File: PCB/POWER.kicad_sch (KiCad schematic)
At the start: 32 parts, among them IC100 AP63203WU-7, J100 2604-3102, Q100 CSD19537Q3, Q101 BSS138, U100 TPS26631RGE

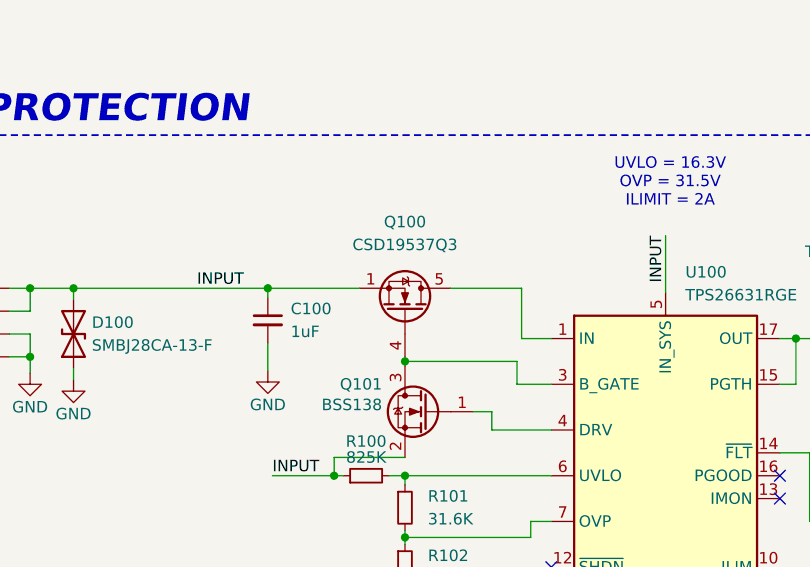
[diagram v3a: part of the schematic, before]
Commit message: PCB acabada con labels
Se agrego:
- Planos de tierra
- Stitching vias
- Labels indicadores para todo los conectores

Se corrigio:
- Errores de librerias de footprint - TPS26631RGE
- Pines sin conectarse
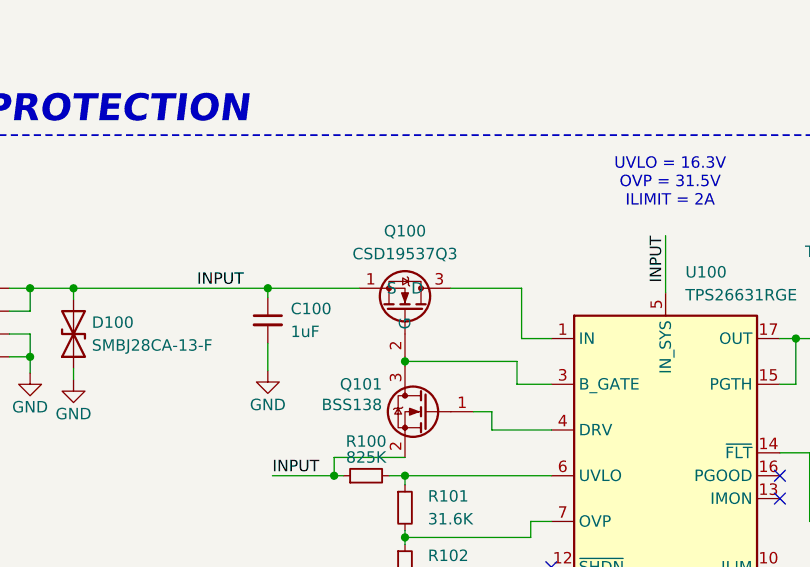
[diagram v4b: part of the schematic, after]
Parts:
- removed Q100: CSD19537Q3, Package_SON:VSON-8_3.3x3.3mm_P0.65mm_NexFET, symbol Transistor_FET:CSD19537Q3
- added Q100: CSD19537Q3, CSD19537Q3:CSD19537Q3, symbol CSD19537Q3:CSD19537Q3
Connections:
- net INPUT: now also Q100.1 (S)
- net at U100.1 (IN), U100.2 (IN): now also Q100.3 (D)
- net at Q101.3 (D), U100.3 (B_GATE): now also Q100.2 (G)
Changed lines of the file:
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@@
 	(wire
 		(pts
+			(xy 84.582 63.754) (xy 92.456 63.754)
+		)
+		(stroke
+			(width 0)
+			(type default)
+		)
+	)
+	(wire
+		(pts
 			(xy 64.262 69.85) (xy 64.262 72.898)
 		)
@@
 	(wire
 		(pts
-			(xy 84.582 63.754) (xy 92.456 63.754)
-		)
-		(stroke
-			(width 0)
-			(type default)
-		)
-	)
-	(wire
-		(pts
 			(xy 250.19 58.42) (xy 250.19 61.722)
 		)
@@
 	)
 	(symbol
-		(lib_id "Transistor_FET:CSD19537Q3")
-		(at 79.502 66.294 270)
-		(mirror x)
-		(unit 1)
-		(exclude_from_sim no)
-		(in_bom yes)
-		(on_board yes)
-		(dnp no)
-		(property "Reference" "Q100"
-			(at 79.502 56.388 90)
-			(effects
-				(font
-					(size 1.27 1.27)
-				)
-			)
-		)
-		(property "Value" "CSD19537Q3"
-			(at 79.502 58.928 90)
-			(effects
-				(font
-					(size 1.27 1.27)
-				)
-			)
-		)
-		(property "Footprint" "Package_SON:VSON-8_3.3x3.3mm_P0.65mm_NexFET"
-			(at 77.597 61.214 0)
-			(effects
-				(font
-					(size 1.27 1.27)
-					(italic yes)
-				)
-				(justify left)
-				(hide yes)
-			)
-		)
-		(property "Datasheet" "http://www.ti.com/lit/ds/symlink/csd19537q3.pdf"
-			(at 75.692 61.214 0)
-			(effects
-				(font
-					(size 1.27 1.27)
-				)
-				(justify left)
-				(hide yes)
-			)
-		)
-		(property "Description" "50A Id, 100V Vds, NexFET N-Channel Power MOSFET, 13mOhm Ron, Qg Typ 16.0nC, VSON8 3.3x3.3mm"
-			(at 79.502 66.294 0)
-			(effects
-				(font
-					(size 1.27 1.27)
-				)
-				(hide yes)
-			)
-		)
-		(property "LCSC" "C478469"
-			(at 79.502 66.294 90)
-			(effects
-				(font
-					(size 1.27 1.27)
-				)
-				(hide yes)
-			)
-		)
-		(pin "3"
-		)
-		(pin "1"
-		)
-		(pin "2"
-		)
-		(pin "5"
-		)
-		(pin "4"
-		)
-		(instances
-			(project ""
-				(path "/118ffa26-3c65-424a-af71-04338c4de0b0/e2751aaa-40ab-491e-8724-b4cb7cd2712b"
-					(reference "Q100")
-					(unit 1)
-				)
-			)
-		)
-	)
-	(symbol
 		(lib_id "power:GND")
 		(at 157.734 83.82 0)
@@
 					(unit 1)
 				)
+			)
+		)
+	)
+	(symbol
+		(lib_id "CSD19537Q3:CSD19537Q3")
+		(at 79.502 81.534 270)
+		(mirror x)
+		(unit 1)
+		(exclude_from_sim no)
+		(in_bom yes)
+		(on_board yes)
+		(dnp no)
+		(property "Reference" "Q100"
+			(at 79.502 57.404 90)
+			(effects
+				(font
+					(size 1.27 1.27)
+				)
+			)
+		)
+		(property "Value" "CSD19537Q3"
+			(at 79.502 59.944 90)
+			(effects
+				(font
+					(size 1.27 1.27)
+				)
+			)
+		)
+		(property "Footprint" "CSD19537Q3:CSD19537Q3"
+			(at -15.418 59.944 0)
+			(effects
+				(font
+					(size 1.27 1.27)
+				)
+				(justify left top)
+				(hide yes)
+			)
+		)
+		(property "Datasheet" "http://www.ti.com/lit/gpn/csd19537q3"
+			(at -115.418 59.944 0)
+			(effects
+				(font
+					(size 1.27 1.27)
+				)
+				(justify left top)
+				(hide yes)
+			)
+		)
+		(property "Description" "100V, N ch NexFET MOSFET, single SON3x3, 14.5mOhm"
+			(at 79.502 81.534 0)
+			(effects
+				(font
+					(size 1.27 1.27)
+				)
+				(hide yes)
+			)
+		)
+		(property "Height" ""
+			(at -315.418 59.944 0)
+			(effects
+				(font
+					(size 1.27 1.27)
+				)
+				(justify left top)
+				(hide yes)
+			)
+		)
+		(property "Mouser Part Number" "595-CSD19537Q3"
+			(at -415.418 59.944 0)
+			(effects
+				(font
+					(size 1.27 1.27)
+				)
+				(justify left top)
+				(hide yes)
+			)
+		)
+		(property "Mouser Price/Stock" "https://www.mouser.co.uk/ProductDetail/Texas-Instruments/CSD19537Q3?qs=kFLL9AfgRSA2baK1OoK3Jg%3D%3D"
+			(at -515.418 59.944 0)
+			(effects
+				(font
+					(size 1.27 1.27)
+				)
+				(justify left top)
+				(hide yes)
+			)
+		)
+		(property "Manufacturer_Name" "Texas Instruments"
+			(at -615.418 59.944 0)
+			(effects
+				(font
+					(size 1.27 1.27)
+				)
+				(justify left top)
+				(hide yes)
+			)
+		)
+		(property "Manufacturer_Part_Number" "CSD19537Q3"
+			(at -715.418 59.944 0)
+			(effects
+				(font
+					(size 1.27 1.27)
+				)
+				(justify left top)
+				(hide yes)
+			)
+		)
+		(property "LCSC" "C478469"
+			(at 79.502 81.534 90)
+			(effects
+				(font
+					(size 1.27 1.27)
+				)
+				(hide yes)
+			)
+		)
+		(pin "1"
+		)
+		(pin "3"
+		)
+		(pin "2"
+		)
+		(instances
+			(project ""
+				(path "/118ffa26-3c65-424a-af71-04338c4de0b0/e2751aaa-40ab-491e-8724-b4cb7cd2712b"
+					(reference "Q100")
+					(unit 1)
+				)

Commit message: Edicion de archivos para JLCPCB
Se ha realizado:
- Cambio de footprint de capacitor 1mF
- Edicion de algunos value references
- Creación de archivos para JLCPCB
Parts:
- C102: footprint Capacitor_SMD:CP_Elec_16x17.5 -> VKMI1701H102MV:VKMI1701H102MV
- Q101: LCSC C7420339 -> C40912
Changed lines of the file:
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@@
 			)
 		)
-		(property "Footprint" "Capacitor_SMD:CP_Elec_16x17.5"
+		(property "Footprint" "VKMI1701H102MV:VKMI1701H102MV"
 			(at 128.778 73.152 0)
 			(effects
@@
 			)
 		)
-		(property "LCSC" "C7420339"
+		(property "LCSC" "C40912"
 			(at 82.042 77.47 0)
 			(effects

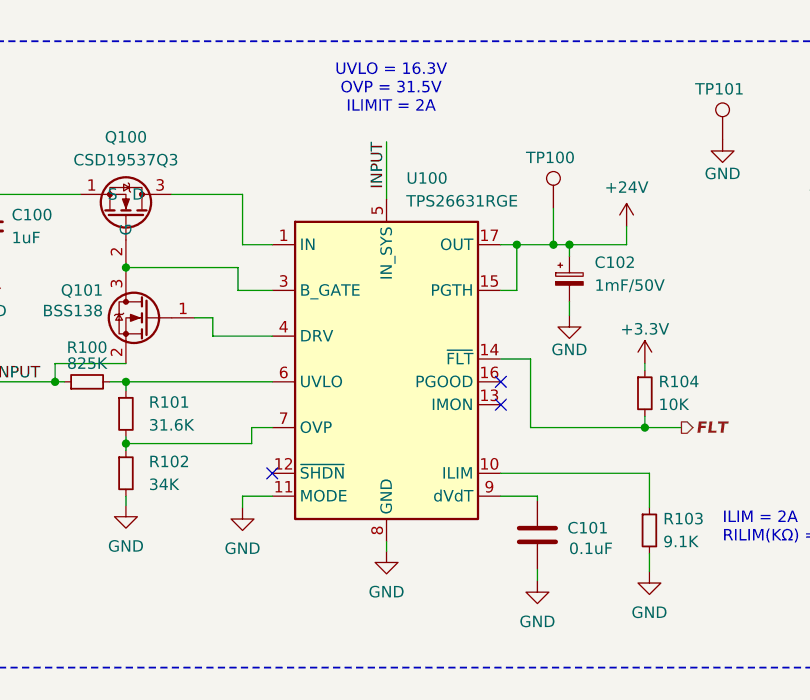
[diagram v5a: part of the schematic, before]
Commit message: Cambio de footprint del eFuse
- Se cambio el footprint del eFuse debido a que el actual no hay stock en JLCPCB
- Se creo de nuevo los archivos de configuracion de JLCPCB
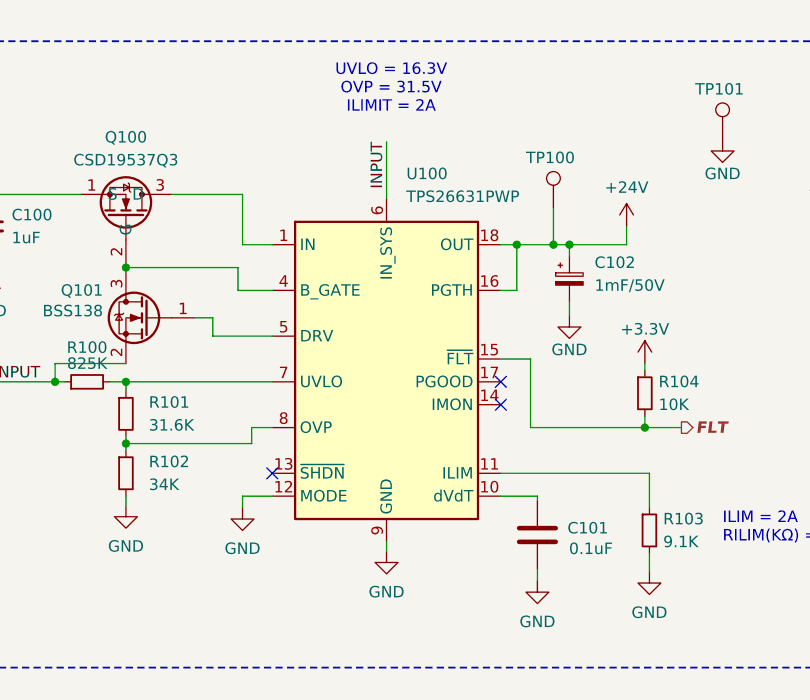
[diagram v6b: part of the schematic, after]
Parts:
- removed U100: TPS26631RGE, Package_DFN_QFN:Texas_RGE0024H_VQFN-24-1EP_4x4mm_P0.5mm_EP2.7x2.7mm_ThermalVias, symbol Power_Management:TPS26631RGE
- added U100: TPS26631PWP, Package_SO:HTSSOP-20-1EP_4.4x6.5mm_P0.65mm_EP3.4x6.5mm_Mask2.96x2.96mm_ThermalVias, symbol Power_Management:TPS26631PWP
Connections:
- net +24V: now also U100.16 (PGTH), U100.18 (OUT), U100.19 (OUT), U100.20 (OUT)
- net FLT: now also U100.15 (~{FLT})
- net GND: now also U100.12 (MODE), U100.21 (GND), U100.9 (GND)
- net INPUT: now also U100.6 (IN_SYS)
- net at R103.1: now also U100.11 (ILIM)
- net at R100.2, R101.1: now also U100.7 (UVLO)
- net at R101.2, R102.1: now also U100.8 (OVP)
- net at Q100.3 (D): now also U100.1 (IN), U100.2 (IN), U100.3 (IN)
- net at Q100.2 (G), Q101.3 (D): now also U100.4 (B_GATE)
- net at Q101.1 (G): now also U100.5 (DRV)
- net at C101.2: now also U100.10 (dVdT)
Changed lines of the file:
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@@
+	)
+	(symbol
+		(lib_id "Power_Management:TPS26631PWP")
+		(at 108.458 82.042 0)
+		(unit 1)
+		(exclude_from_sim no)
+		(in_bom yes)
+		(on_board yes)
+		(dnp no)
+		(fields_autoplaced yes)
+		(property "Reference" "U100"
+			(at 110.6521 61.468 0)
+			(effects
+				(font
+					(size 1.27 1.27)
+				)
+				(justify left)
+			)
+		)
+		(property "Value" "TPS26631PWP"
+			(at 110.6521 64.008 0)
+			(effects
+				(font
+					(size 1.27 1.27)
+				)
+				(justify left)
+			)
+		)
+		(property "Footprint" "Package_SO:HTSSOP-20-1EP_4.4x6.5mm_P0.65mm_EP3.4x6.5mm_Mask2.96x2.96mm_ThermalVias"
+			(at 108.458 113.792 0)
+			(effects
+				(font
+					(size 1.27 1.27)
+				)
+				(hide yes)
+			)
+		)
+		(property "Datasheet" "https://www.ti.com/lit/ds/symlink/tps2663.pdf"
+			(at 98.298 61.722 0)
+			(effects
+				(font
+					(size 1.27 1.27)
+				)
+				(hide yes)
+			)
+		)
+		(property "Description" "60V, 6A Power Limiting, Surge Protection Industrial eFuse, Adjustable Overvoltage cut-off, Active Current Limiting with Pulse current support, HTTSOP-20"
+			(at 108.458 82.042 0)
+			(effects
+				(font
+					(size 1.27 1.27)
+				)
+				(hide yes)
+			)
+		)
+		(property "LCSC" "C2832195"
+			(at 108.458 82.042 0)
+			(effects
+				(font
+					(size 1.27 1.27)
+				)
+				(hide yes)
+			)
+		)
+		(pin "12"
+		)
+		(pin "21"
+		)
+		(pin "5"
+		)
+		(pin "6"
+		)
+		(pin "7"
+		)
+		(pin "15"
+		)
+		(pin "14"
+		)
+		(pin "19"
+		)
+		(pin "9"
+		)
+		(pin "18"
+		)
+		(pin "10"
+		)
+		(pin "20"
+		)
+		(pin "8"
+		)
+		(pin "16"
+		)
+		(pin "1"
+		)
+		(pin "2"
+		)
+		(pin "3"
+		)
+		(pin "11"
+		)
+		(pin "4"
+		)
+		(pin "17"
+		)
+		(pin "13"
+		)
+		(instances
+			(project ""
+				(path "/118ffa26-3c65-424a-af71-04338c4de0b0/e2751aaa-40ab-491e-8724-b4cb7cd2712b"
+					(reference "U100")
+					(unit 1)
+				)
+			)
+		)
 	)
 	(symbol
@@
 					(unit 1)
 				)
-			)
-		)
-	)
-	(symbol
-		(lib_id "Power_Management:TPS26631RGE")
-		(at 108.458 82.042 0)
-		(unit 1)
-		(exclude_from_sim no)
-		(in_bom yes)
-		(on_board yes)
-		(dnp no)
-		(fields_autoplaced yes)
-		(property "Reference" "U100"
-			(at 110.6521 61.976 0)
-			(effects
-				(font
-					(size 1.27 1.27)
-				)
-				(justify left)
-			)
-		)
-		(property "Value" "TPS26631RGE"
-			(at 110.6521 64.516 0)
-			(effects
-				(font
-					(size 1.27 1.27)
-				)
-				(justify left)
-			)
-		)
-		(property "Footprint" "Package_DFN_QFN:Texas_RGE0024H_VQFN-24-1EP_4x4mm_P0.5mm_EP2.7x2.7mm_ThermalVias"
-			(at 108.458 113.792 0)
-			(effects
-				(font
-					(size 1.27 1.27)
-				)
-				(hide yes)
-			)
-		)
-		(property "Datasheet" "https://www.ti.com/lit/ds/symlink/tps2663.pdf"
-			(at 98.298 61.722 0)
-			(effects
-				(font
-					(size 1.27 1.27)
-				)
-				(hide yes)
-			)
-		)
-		(property "Description" "60V, 6A Power Limiting, Surge Protection Industrial eFuse, Adjustable Overvoltage cut-off, Active Current Limiting with Pulse current support, VQFN-24"
-			(at 108.458 82.042 0)
-			(effects
-				(font
-					(size 1.27 1.27)
-				)
-				(hide yes)
-			)
-		)
-		(property "LCSC" "C1850273"
-			(at 108.458 82.042 0)
-			(effects
-				(font
-					(size 1.27 1.27)
-				)
-				(hide yes)
-			)
-		)
-		(pin "11"
-		)
-		(pin "6"
-		)
-		(pin "10"
-		)
-		(pin "21"
-		)
-		(pin "23"
-		)
-		(pin "12"
-		)
-		(pin "9"
-		)
-		(pin "24"
-		)
-		(pin "17"
-		)
-		(pin "2"
-		)
-		(pin "13"
-		)
-		(pin "4"
-		)
-		(pin "7"
-		)
-		(pin "8"
-		)
-		(pin "1"
-		)
-		(pin "19"
-		)
-		(pin "22"
-		)
-		(pin "14"
-		)
-		(pin "18"
-		)
-		(pin "25"
-		)
-		(pin "5"
-		)
-		(pin "15"
-		)
-		(pin "3"
-		)
-		(pin "16"
-		)
-		(pin "20"
-		)
-		(instances
-			(project "PCB-Cuarto"
-				(path "/118ffa26-3c65-424a-af71-04338c4de0b0/e2751aaa-40ab-491e-8724-b4cb7cd2712b"
-					(reference "U100")
-					(unit 1)
-				)

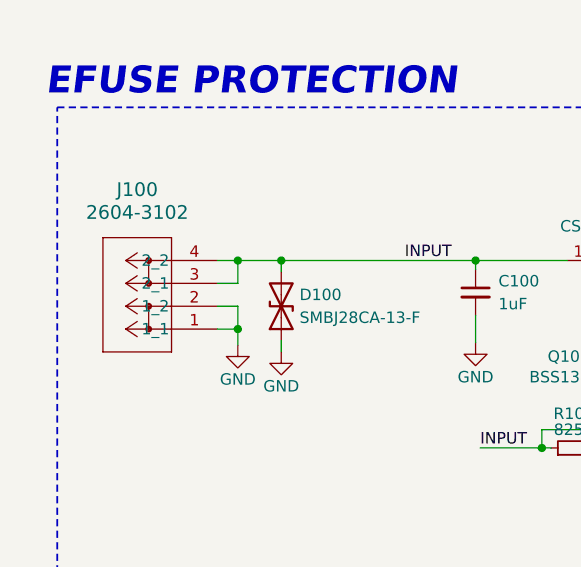
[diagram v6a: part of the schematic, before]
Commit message: Change Placement
Se ha cambiado el placement total para obtener una mejor posicion de conexion de los perifericos
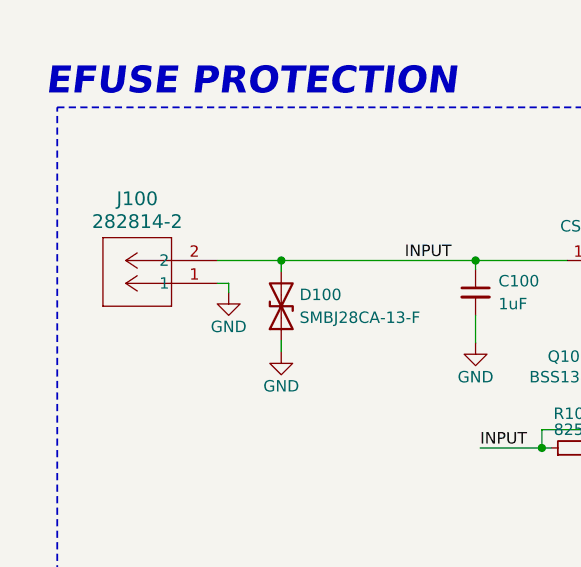
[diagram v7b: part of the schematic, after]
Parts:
- removed J100: 2604-3102, 2604-3102:2604-3102, symbol 2604-3102:2604-3102
- added J100: 282814-2, 282814-2:282814-2, symbol 282814-2:282814-2
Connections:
- net GND: now also J100.1
- net INPUT: now also J100.2
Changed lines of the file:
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@@
-	)
-	(junction
-		(at 37.846 71.374)
-		(diameter 0)
-		(color 0 0 0 0)
 	)
 	(junction
@@
 	)
 	(junction
-		(at 37.846 63.754)
-		(diameter 0)
-		(color 0 0 0 0)
-	)
-	(junction
 		(at 79.502 71.882)
 		(diameter 0)
@@
 	(wire
 		(pts
-			(xy 37.846 66.294) (xy 37.846 63.754)
-		)
-		(stroke
-			(width 0)
-			(type default)
-		)
-	)
-	(wire
-		(pts
 			(xy 64.262 63.754) (xy 74.422 63.754)
 		)
@@
 	(wire
 		(pts
-			(xy 35.56 63.754) (xy 37.846 63.754)
+			(xy 35.56 63.754) (xy 42.672 63.754)
 		)
 		(stroke
@@
 	(wire
 		(pts
-			(xy 35.56 71.374) (xy 37.846 71.374)
-		)
-		(stroke
-			(width 0)
-			(type default)
-		)
-	)
-	(wire
-		(pts
 			(xy 79.502 84.582) (xy 79.502 85.598)
 		)
@@
 	(wire
 		(pts
-			(xy 35.56 66.294) (xy 37.846 66.294)
-		)
-		(stroke
-			(width 0)
-			(type default)
-		)
-	)
-	(wire
-		(pts
 			(xy 201.422 61.722) (xy 206.248 61.722)
 		)
@@
 	(wire
 		(pts
+			(xy 36.83 66.294) (xy 36.83 67.31)
+		)
+		(stroke
+			(width 0)
+			(type default)
+		)
+	)
+	(wire
+		(pts
 			(xy 121.158 69.342) (xy 122.936 69.342)
 		)
@@
 	(wire
 		(pts
-			(xy 37.846 71.374) (xy 37.846 73.152)
-		)
-		(stroke
-			(width 0)
-			(type default)
-		)
-	)
-	(wire
-		(pts
 			(xy 196.85 120.65) (xy 199.39 120.65)
 		)
@@
 	(wire
 		(pts
-			(xy 35.56 68.834) (xy 37.846 68.834)
-		)
-		(stroke
-			(width 0)
-			(type default)
-		)
-	)
-	(wire
-		(pts
 			(xy 79.502 71.882) (xy 79.502 72.39)
 		)
@@
 	(wire
 		(pts
-			(xy 37.846 63.754) (xy 42.672 63.754)
-		)
-		(stroke
-			(width 0)
-			(type default)
-		)
-	)
-	(wire
-		(pts
 			(xy 124.46 82.042) (xy 124.46 89.662)
 		)
@@
 	(wire
 		(pts
+			(xy 35.56 66.294) (xy 36.83 66.294)
+		)
+		(stroke
+			(width 0)
+			(type default)
+		)
+	)
+	(wire
+		(pts
 			(xy 128.778 69.342) (xy 135.128 69.342)
 		)
@@
 		(pts
 			(xy 121.158 94.742) (xy 137.668 94.742)
-		)
-		(stroke
-			(width 0)
-			(type default)
-		)
-	)
-	(wire
-		(pts
-			(xy 37.846 68.834) (xy 37.846 71.374)
 		)
 		(stroke
@@
 	)
 	(symbol
+		(lib_id "282814-2:282814-2")
+		(at 35.56 66.294 180)
+		(unit 1)
+		(exclude_from_sim no)
+		(in_bom yes)
+		(on_board yes)
+		(dnp no)
+		(fields_autoplaced yes)
+		(property "Reference" "J100"
+			(at 26.67 56.896 0)
+			(effects
+				(font
+					(size 1.524 1.524)
+				)
+			)
+		)
+		(property "Value" "282814-2"
+			(at 26.67 59.436 0)
+			(effects
+				(font
+					(size 1.524 1.524)
+				)
+			)
+		)
+		(property "Footprint" "282814-2:282814-2"
+			(at 35.56 66.294 0)
+			(effects
+				(font
+					(size 1.27 1.27)
+					(italic yes)
+				)
+				(hide yes)
+			)
+		)
+		(property "Datasheet" "https://www.te.com/commerce/DocumentDelivery/DDEController?Action=srchrtrv&DocNm=1-1773458-1_EURO_STYLE_QRG&DocType=Data+Sheet&DocLang=English&PartCntxt=282814-2&DocFormat=pdf"
+			(at 35.56 66.294 0)
+			(effects
+				(font
+					(size 1.27 1.27)
+					(italic yes)
+				)
+				(hide yes)
+			)
+		)
+		(property "Description" ""
+			(at 35.56 66.294 0)
+			(effects
+				(font
+					(size 1.27 1.27)
+				)
+				(hide yes)
+			)
+		)
+		(property "LCSC" "C5187973"
+			(at 35.56 66.294 0)
+			(effects
+				(font
+					(size 1.27 1.27)
+				)
+				(hide yes)
+			)
+		)
+		(pin "2"
+		)
+		(pin "1"
+		)
+		(instances
+			(project ""
+				(path "/118ffa26-3c65-424a-af71-04338c4de0b0/e2751aaa-40ab-491e-8724-b4cb7cd2712b"
+					(reference "J100")
+					(unit 1)
+				)
+			)
+		)
+	)
+	(symbol
 		(lib_id "Device:R_Small")
 		(at 137.16 85.852 0)
@@
 	(symbol
 		(lib_id "power:GND")
-		(at 37.846 73.152 0)
+		(at 36.83 67.31 0)
 		(unit 1)
 		(exclude_from_sim no)
@@
 		(dnp no)
 		(property "Reference" "#PWR01"
-			(at 37.846 79.502 0)
+			(at 36.83 73.66 0)
 			(effects
 				(font
@@
 		)
 		(property "Value" "GND"
-			(at 37.846 76.962 0)
+			(at 36.83 71.12 0)
 			(effects
 				(font
@@
 		)
 		(property "Footprint" ""
-			(at 37.846 73.152 0)
+			(at 36.83 67.31 0)
 			(effects
 				(font
@@
 		)
 		(property "Datasheet" ""
-			(at 37.846 73.152 0)
+			(at 36.83 67.31 0)
 			(effects
 				(font
@@
 		)
 		(property "Description" "Power symbol creates a global label with name \"GND\" , ground"
-			(at 37.846 73.152 0)
+			(at 36.83 67.31 0)
 			(effects
 				(font
@@
 					(unit 1)
 				)
-			)
-		)
-	)
-	(symbol
-		(lib_id "2604-3102:2604-3102")
-		(at 35.56 71.374 180)
-		(unit 1)
-		(exclude_from_sim no)
-		(in_bom yes)
-		(on_board yes)
-		(dnp no)
-		(fields_autoplaced yes)
-		(property "Reference" "J100"
-			(at 26.67 55.88 0)
-			(effects
-				(font
-					(size 1.524 1.524)
-				)
-			)
-		)
-		(property "Value" "2604-3102"
-			(at 26.67 58.42 0)
-			(effects
-				(font
-					(size 1.524 1.524)
-				)
-			)
-		)
-		(property "Footprint" "2604-3102:2604-3102"
-			(at 35.56 71.374 0)
-			(effects
-				(font
-					(size 1.27 1.27)
-					(italic yes)
-				)
-				(hide yes)
-			)
-		)
-		(property "Datasheet" "2604-3102"
-			(at 35.56 71.374 0)
-			(effects
-				(font
-					(size 1.27 1.27)
-					(italic yes)
-				)
-				(hide yes)
-			)
-		)
-		(property "Description" ""
-			(at 35.56 71.374 0)
-			(effects
-				(font
-					(size 1.27 1.27)
-				)
-				(hide yes)
-			)
-		)
-		(pin "4"
-		)
-		(pin "3"
-		)
-		(pin "2"
-		)
-		(pin "1"
-		)
-		(instances
-			(project ""
-				(path "/118ffa26-3c65-424a-af71-04338c4de0b0/e2751aaa-40ab-491e-8724-b4cb7cd2712b"
-					(reference "J100")
-					(unit 1)
-				)
